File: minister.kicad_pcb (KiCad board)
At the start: 2 copper layers, 271.5 x 88.1 mm, 108 parts, among them SW1 SW_Push, U1 ATmega32U4-AU, Y1 16MHz

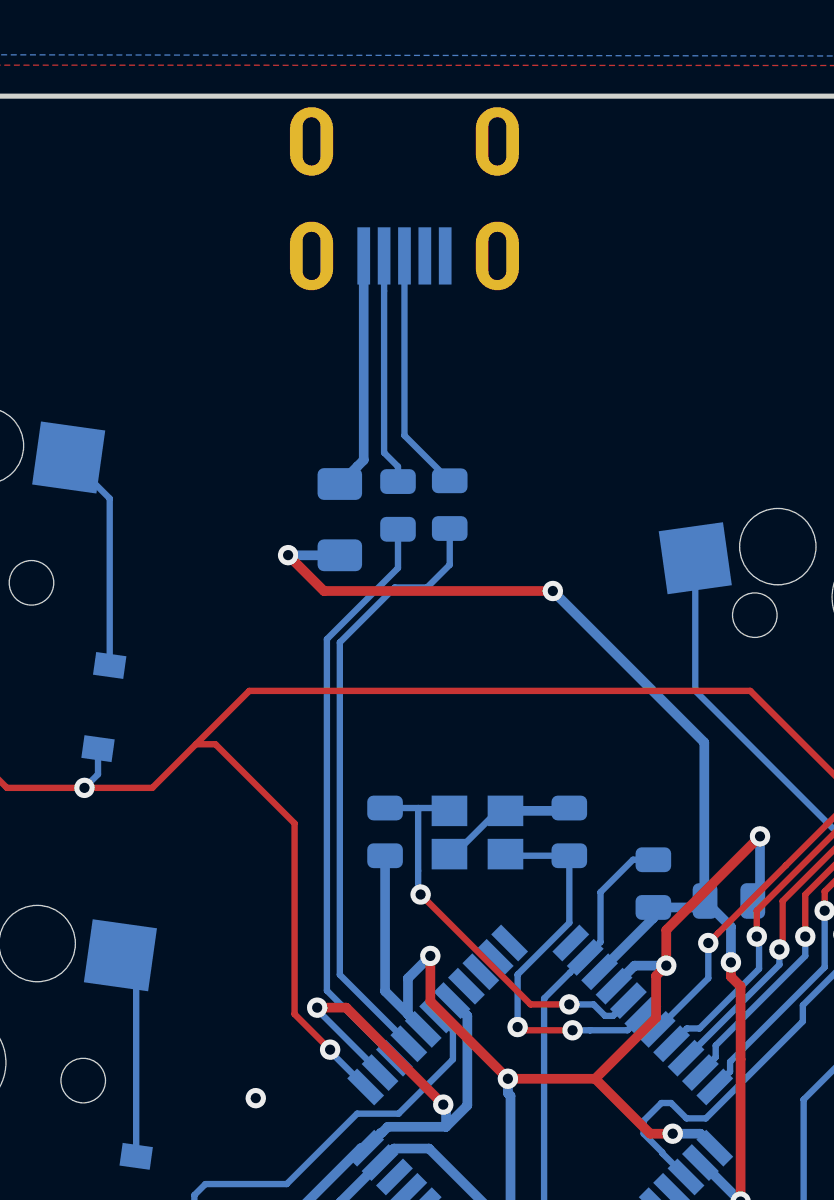
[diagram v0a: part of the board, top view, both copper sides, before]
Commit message: replace usb and generate output files
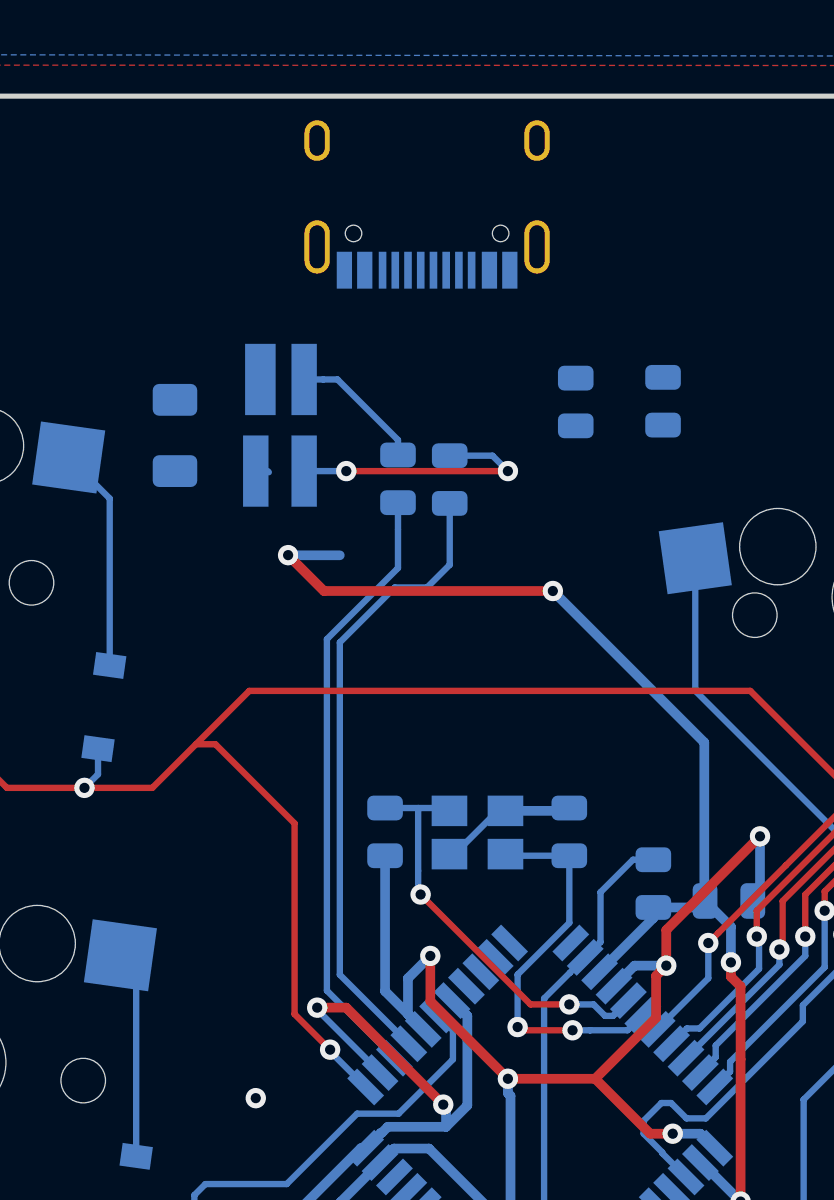
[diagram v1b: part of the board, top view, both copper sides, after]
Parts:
- removed R2, R3: 22, Resistor_SMD:R_0805_2012Metric
- added D47: PRTR5V0U2X, Package_TO_SOT_SMD:SOT-143_Handsoldering, B.Cu at (134.0, 79.5)
- added R5: 5.1k, Resistor_SMD:R_0805_2012Metric, B.Cu at (149.1, 78.5)
- added R6: 22, Resistor_SMD:R_0805_2012Metric, B.Cu at (138.7, 81.6)
- added R7: 22, Resistor_SMD:R_0805_2012Metric, B.Cu at (140.7, 81.6)
- added R8: 5.1k, Resistor_SMD:R_0805_2012Metric, B.Cu at (145.7, 78.6)
- F1: value 500mA -> Polyfuse_Small
- USB1: value Molex-0548190589 -> HRO-TYPE-C-31-M-12; footprint random-keyboard-parts:Molex-0548190589 -> Connector_USB:USB_C_Receptacle_HRO_TYPE-C-31-M-12
- moved F1 7.27 mm to (129.9, 79.9), turned to 270 degrees
- moved USB1 1.35 mm to (139.8, 69.3), turned to 0 degrees
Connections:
- F1 pad 2: VCC -> Net-(D47-Pad4)
- U1 pad 3: Net-(R3-Pad1) -> D-
- U1 pad 4: Net-(R2-Pad1) -> D+
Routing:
- net Net-(R2-Pad1): track 23.9 -> 0.00 mm
- net Net-(R3-Pad1): track 23.0 -> 0.00 mm
- net D+: track 9.57 -> 24.9 mm
- net D-: track 9.09 -> 24.1 mm
- net ESD2: track 0.00 -> 10.8 mm, vias 0 -> 2
- net VCC: track 9.35 -> 0.00 mm
- net ESD1: track 0.00 -> 5.26 mm

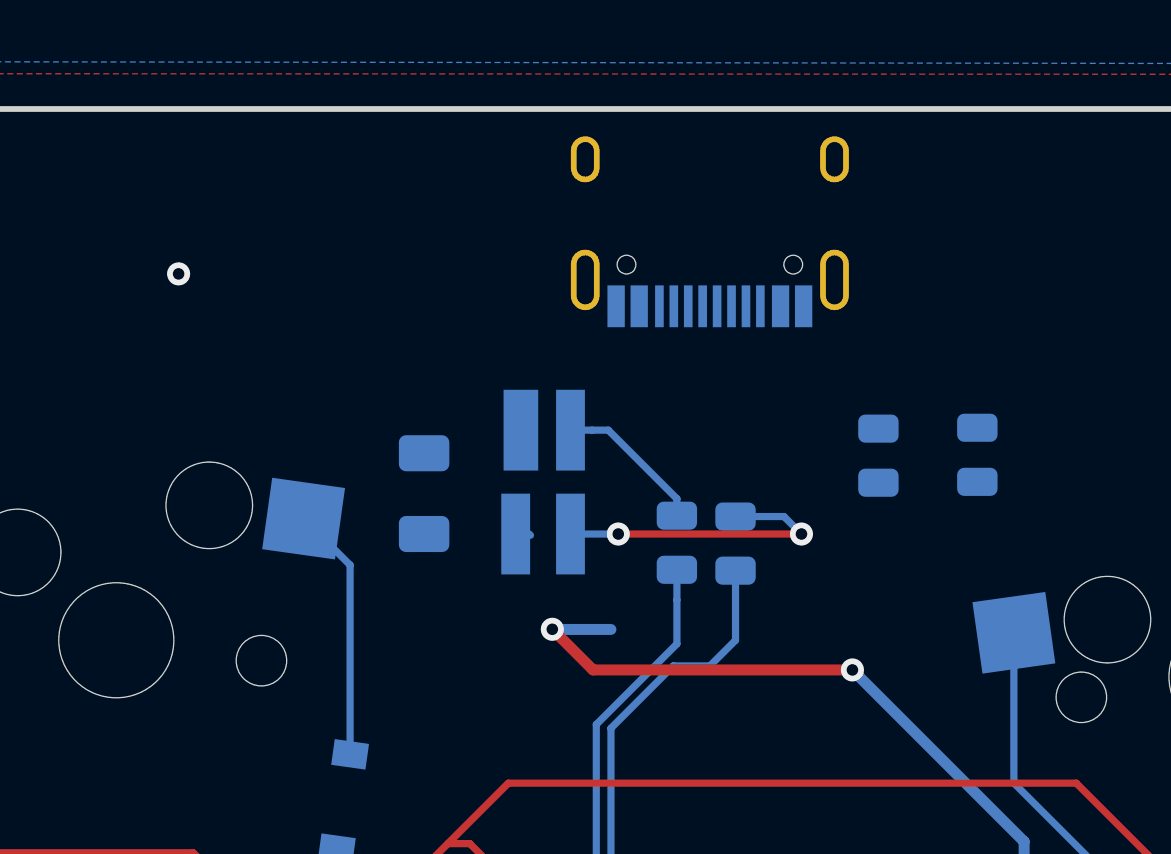
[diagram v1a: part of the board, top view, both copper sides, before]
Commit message: clean up slik screen
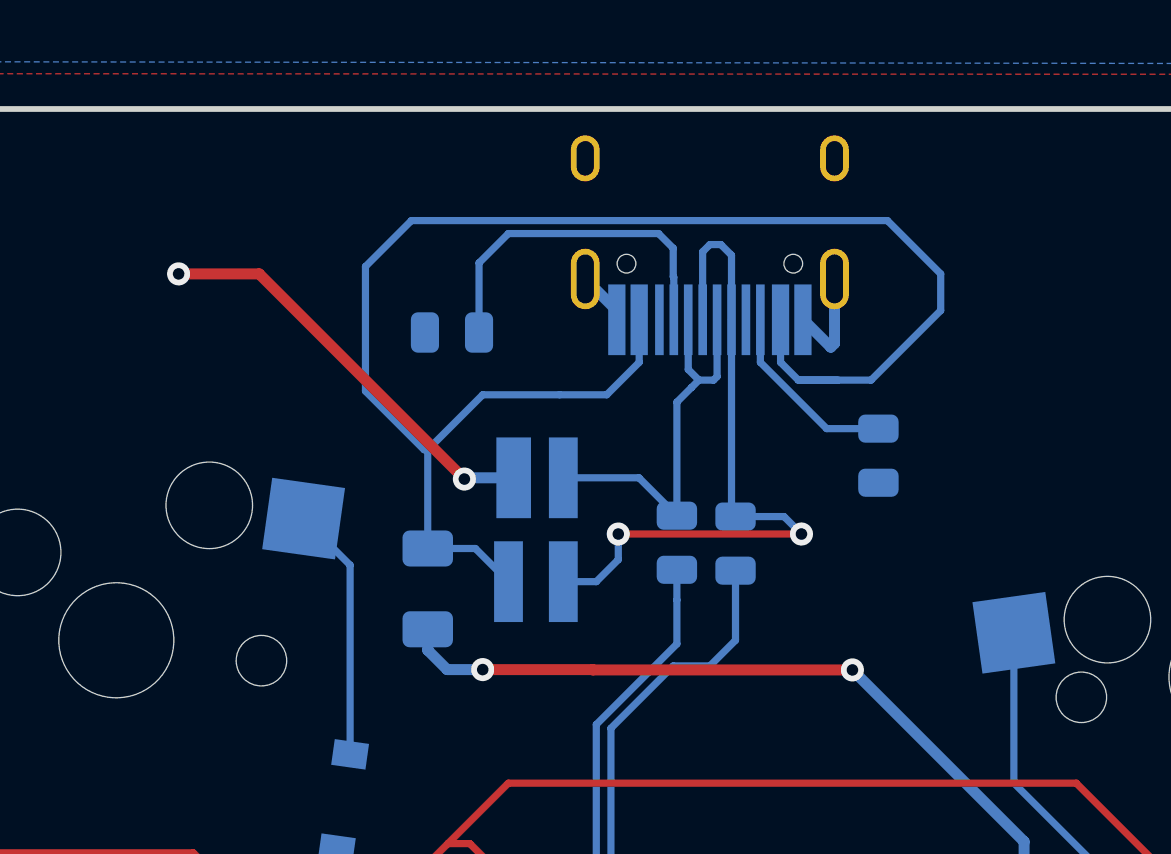
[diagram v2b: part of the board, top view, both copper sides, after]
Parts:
- USB1: footprint Connector_USB:USB_C_Receptacle_HRO_TYPE-C-31-M-12 -> Type-C:HRO-TYPE-C-31-M-12-HandSoldering
- moved R5 18.7 mm to (130.9, 74.3), turned to 0 degrees
- moved USB1 3.68 mm to (139.8, 65.7)
- moved F1 3.30 mm to (130.0, 83.2), turned to 90 degrees
- moved D47 1.67 mm to (133.8, 81.1)
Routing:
- net Net-(D47-Pad4): track 0.06 -> 56.4 mm
- net GND: track 113.4 -> 133.6 mm, vias 11 -> 12
- net ESD2: track 10.8 -> 25.0 mm
- net Net-(R5-Pad2): track 0.00 -> 12.3 mm
- net ESD1: track 5.26 -> 14.4 mm
- net Net-(R8-Pad2): track 0.00 -> 6.52 mm
- net +5V: track 111.0 -> 113.7 mm

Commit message: add isp
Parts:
- added J1: AVR-ISP-6, Connector_IDC:IDC-Header_2x03_P2.54mm_Vertical, F.Cu at (156.5, 73.2)
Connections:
- net Net-(R1-Pad2) renamed RST
- U1 pad 10: Net-(U1-Pad10) -> MOSI
- U1 pad 11: Net-(U1-Pad11) -> MISO
- U1 pad 9: Net-(U1-Pad9) -> SCK
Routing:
- net MOSI: track 0.00 -> 46.5 mm, vias 0 -> 3
- net SCK: track 0.00 -> 38.9 mm, vias 0 -> 2
- net MISO: track 0.00 -> 34.2 mm, vias 0 -> 3
- net RST: track 45.3 -> 78.4 mm
- net +5V: track 113.7 -> 138.1 mm, vias 8 -> 9
- net GND: track 133.6 -> 148.8 mm, vias 12 -> 15

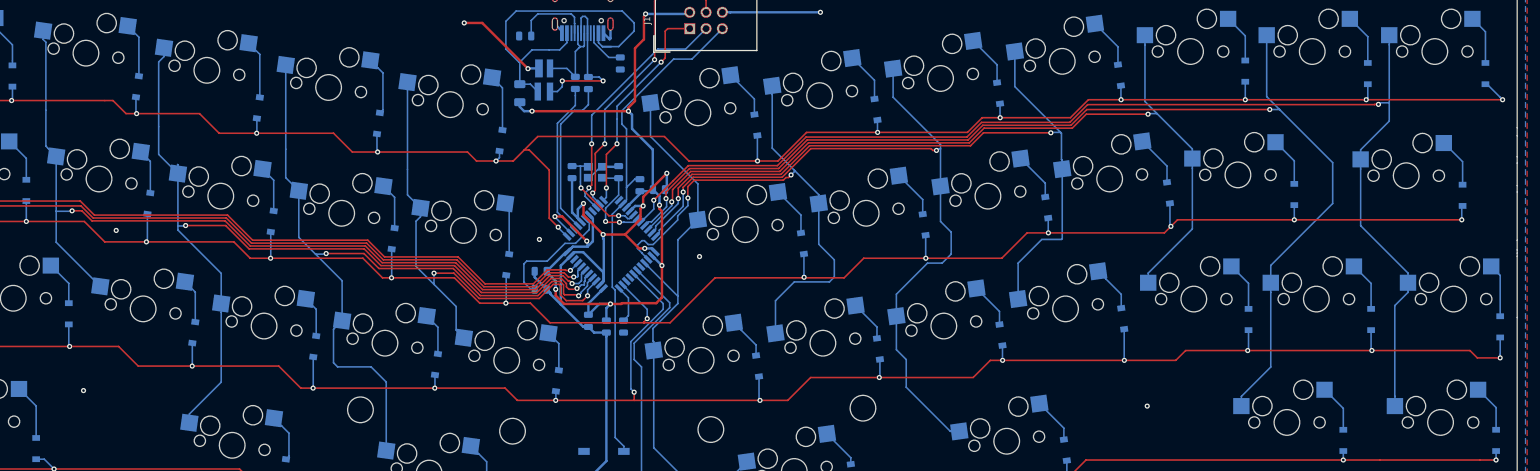
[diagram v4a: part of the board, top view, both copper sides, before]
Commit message: submit for production
generate gerbers and drill files
generate bom and placement file
update some parts
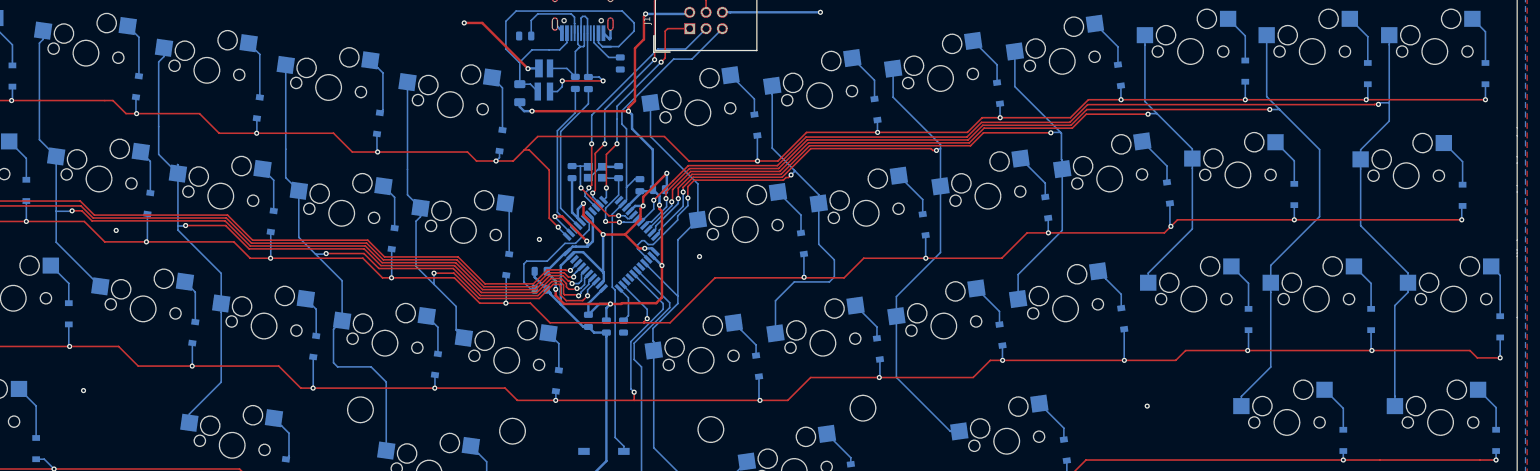
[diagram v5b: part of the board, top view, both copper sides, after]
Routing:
- net ROW0: track 311.6 -> 307.9 mm
- net COL8: track 122.0 -> 119.3 mm
- net COL9: track 117.9 -> 116.1 mm
- net COL11: track 175.5 -> 173.8 mm
- net GND: track 148.8 -> 147.6 mm
- net COL1: track 172.9 -> 173.8 mm
- net D+: track 24.9 -> 24.1 mm
